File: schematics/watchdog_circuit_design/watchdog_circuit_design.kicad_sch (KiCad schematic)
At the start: 25 parts, among them SW1 Config mode

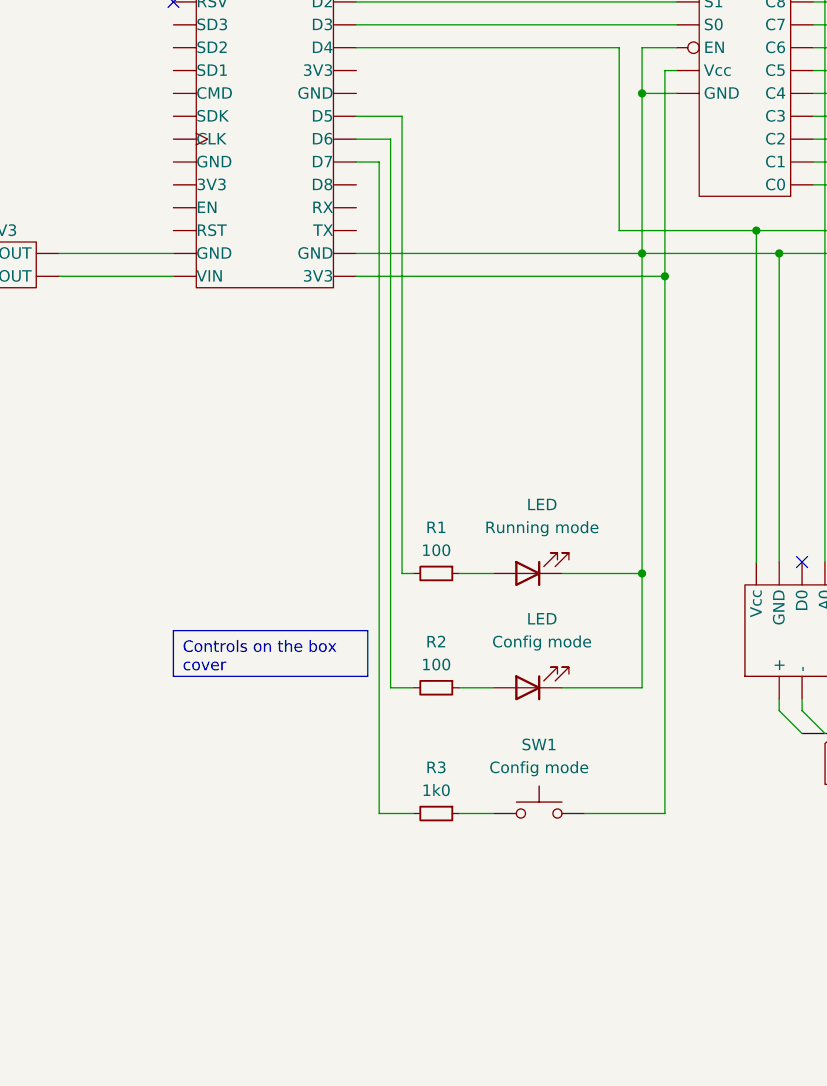
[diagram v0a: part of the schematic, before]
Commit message: Add "WiFi connected LED" to the Watchdog unit schema
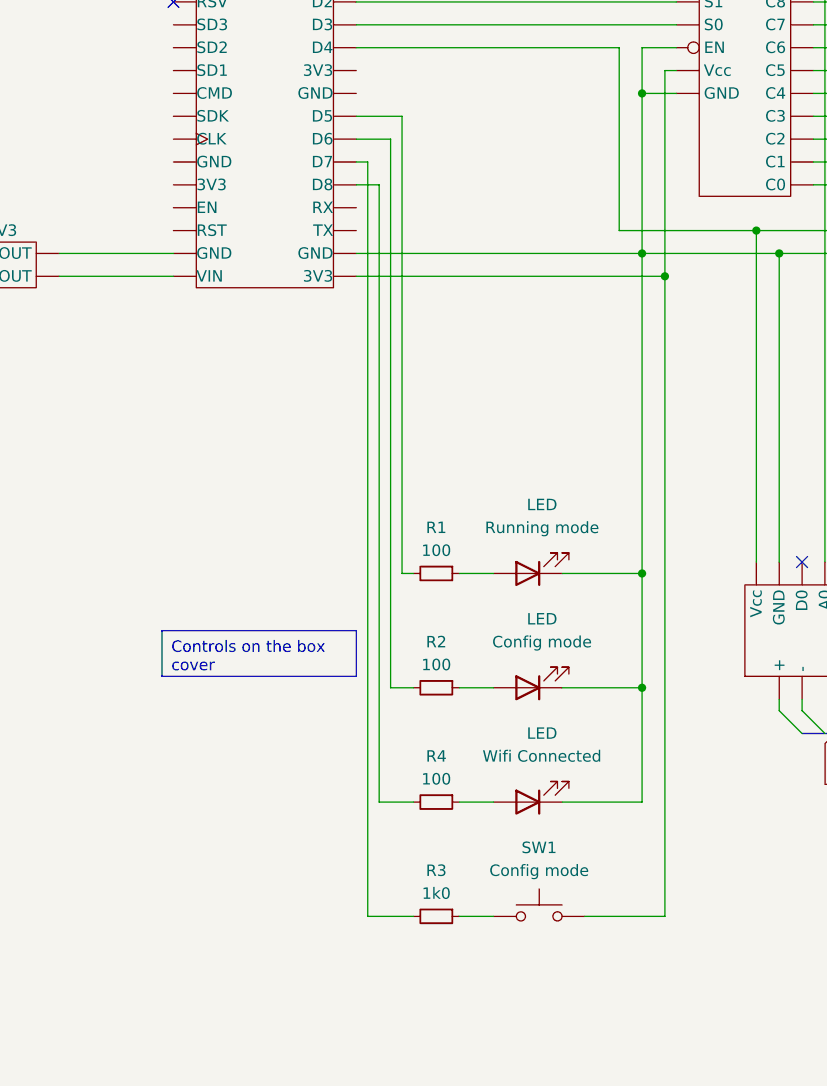
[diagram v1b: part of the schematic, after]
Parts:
- added LED: Wifi Connected, symbol Device:LED
- added R4: 100, symbol Device:R_Small
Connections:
- net at U10. (Vcc): now also MUX. (Vcc)
- net at MUX. (Vcc): now also U5. (Vcc); no longer U10. (Vcc)
- net at U3. (Vcc): now also MUX. (Vcc)
- net at U1. (Vcc): now also MUX. (Vcc)
- net at U12. (Vcc): now also MUX. (Vcc)
- net at U6. (Vcc): no longer MUX. (Vcc)
- net at U2. (Vcc): no longer MUX. (Vcc)
- net at U15. (Vcc): no longer MUX. (Vcc)
- net at U16. (Vcc): no longer MUX. (Vcc)
- net at U13. (Vcc): no longer MUX. (Vcc)
- net at U4. (Vcc): no longer MUX. (Vcc)
- net at U11. (Vcc): no longer MUX. (Vcc)
- net at U9. (Vcc): no longer MUX. (Vcc)
- net at U7. (Vcc): no longer MUX. (Vcc)
- net at U14. (Vcc): no longer MUX. (Vcc)
- net at U8. (Vcc): no longer MUX. (Vcc)
- net at U5. (Vcc): no longer MUX. (Vcc)
- new net: LED.1 (K), LED.1 (K), LED.1 (K), MUX. (Vcc), U1. (Vcc), U10. (Vcc), U11. (Vcc), U12. (Vcc), U13. (Vcc), U14. (Vcc), U15. (Vcc), U16. (Vcc), U2. (Vcc), U3. (Vcc), U4. (Vcc), U5. (Vcc), U6. (Vcc), U7. (Vcc), U8. (Vcc), U9. (Vcc), uC. (VIN)
- new net: U1. (Vcc), U10. (Vcc), U11. (Vcc), U12. (Vcc), U13. (Vcc), U14. (Vcc), U15. (Vcc), U16. (Vcc), U2. (Vcc), U3. (Vcc), U4. (Vcc), U5. (Vcc), U6. (Vcc), U7. (Vcc), U8. (Vcc), U9. (Vcc), uC. (VIN)
- new net: MUX. (Vcc), uC. (VIN) (x5)
- new net: MUX. (Vcc), SW1.2, uC. (VIN)
- new net: R4.2, uC. (VIN)
- new net: VIN->3V3. (-OUT), uC. (VIN) (x2)
- new net: MUX. (Vcc), U6. (Vcc)
- new net: MUX. (Vcc), U2. (Vcc)
- new net: MUX. (Vcc), U15. (Vcc)
- new net: MUX. (Vcc), U16. (Vcc)
- new net: MUX. (Vcc), U13. (Vcc)
- new net: MUX. (Vcc), U4. (Vcc)
- new net: MUX. (Vcc), U11. (Vcc)
- new net: MUX. (Vcc), U9. (Vcc)
- new net: MUX. (Vcc), U7. (Vcc)
- new net: MUX. (Vcc), U14. (Vcc)
- new net: MUX. (Vcc), U8. (Vcc)
- new net: LED.2 (A), R4.1
- now unconnected: U11. (Vcc), U11. (Vcc), U13. (Vcc), U13. (Vcc), U14. (Vcc), U14. (Vcc), U15. (Vcc), U15. (Vcc), U16. (Vcc), U16. (Vcc), U2. (Vcc), U2. (Vcc), U4. (Vcc), U4. (Vcc), U5. (Vcc), U5. (Vcc), U6. (Vcc), U6. (Vcc), U7. (Vcc), U7. (Vcc), U8. (Vcc), U8. (Vcc), U9. (Vcc), U9. (Vcc)
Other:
- moved on the sheet: SW1
